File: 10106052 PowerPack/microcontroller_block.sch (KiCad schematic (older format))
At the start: 29 parts, among them J12 Molex_52207-1933_1x19-1MP_P1.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, J13 S5B-ZR-SM4A-TF, U4 PIC18F43K22T-IPT

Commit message: PowerPack schematic toplevel done
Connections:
- net DISCH_BAT1: no longer U4.23 (RA4/AN4/CAP3/QEB)
- new net DISCH_BAT2: U4.23 (RA4/AN4/CAP3/QEB)
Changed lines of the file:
@@
 $Descr A4 11693 8268
 encoding utf-8
-Sheet 6 7
-Title ""
-Date ""
-Rev ""
+Sheet 4 4
+Title "Microcontroller block"
+Date "2020-04-05"
+Rev "1"
 Comp ""
 Comment1 ""
@@
 $EndComp
 $Comp
-L 10106052_PowerPack:+VDC_PERM #PWR?
+L 10106052_PowerPack:+VDC_PERM #PWR0132
 U 1 1 5E9422DF
 P 10350 3450
-F 0 "#PWR?" H 10350 3300 50  0001 C CNN
+F 0 "#PWR0132" H 10350 3300 50  0001 C CNN
 F 1 "+VDC_PERM" V 10365 3577 50  0000 L CNN
 F 2 "" H 10350 3450 50  0001 C CNN
@@
 $EndComp
 $Comp
-L power:+5V #PWR?
+L power:+5V #PWR0133
 U 1 1 5E942FF6
 P 10350 3250
-F 0 "#PWR?" H 10350 3100 50  0001 C CNN
+F 0 "#PWR0133" H 10350 3100 50  0001 C CNN
 F 1 "+5V" V 10365 3378 50  0000 L CNN
 F 2 "" H 10350 3250 50  0001 C CNN
@@
 $EndComp
 $Comp
-L power:GND #PWR?
+L power:GND #PWR0134
 U 1 1 5E958B97
 P 10250 2350
-F 0 "#PWR?" H 10250 2100 50  0001 C CNN
+F 0 "#PWR0134" H 10250 2100 50  0001 C CNN
 F 1 "GND" V 10255 2222 50  0000 R CNN
 F 2 "" H 10250 2350 50  0001 C CNN
@@
 $EndComp
 $Comp
-L power:GND #PWR?
+L power:GND #PWR0135
 U 1 1 5E951987
 P 10550 6100
-F 0 "#PWR?" H 10550 5850 50  0001 C CNN
+F 0 "#PWR0135" H 10550 5850 50  0001 C CNN
 F 1 "GND" H 10555 5927 50  0000 C CNN
 F 2 "" H 10550 6100 50  0001 C CNN
@@
 $EndComp
 $Comp
-L power:GND #PWR?
+L power:GND #PWR0136
 U 1 1 5E944184
 P 7400 6150
-F 0 "#PWR?" H 7400 5900 50  0001 C CNN
+F 0 "#PWR0136" H 7400 5900 50  0001 C CNN
 F 1 "GND" H 7405 5977 50  0000 C CNN
 F 2 "" H 7400 6150 50  0001 C CNN
@@
 $EndComp
 $Comp
-L power:GNDA #PWR?
+L power:GNDA #PWR0137
 U 1 1 5E93FC0C
 P 9450 6100
-F 0 "#PWR?" H 9450 5850 50  0001 C CNN
+F 0 "#PWR0137" H 9450 5850 50  0001 C CNN
 F 1 "GNDA" H 9455 5927 50  0000 C CNN
 F 2 "" H 9450 6100 50  0001 C CNN
@@
 $EndComp
 $Comp
-L 10106052_PowerPack:+3.0VREF #PWR?
+L 10106052_PowerPack:+3.0VREF #PWR0138
 U 1 1 5EA046DC
 P 2300 4350
-F 0 "#PWR?" H 2300 4200 50  0001 C CNN
+F 0 "#PWR0138" H 2300 4200 50  0001 C CNN
 F 1 "+3.0VREF" V 2315 4478 50  0000 L CNN
 F 2 "" H 2300 4350 50  0001 C CNN
@@
 $EndComp
 $Comp
-L power:+5V #PWR?
+L power:+5V #PWR0139
 U 1 1 5EA2A611
 P 1400 1600
-F 0 "#PWR?" H 1400 1450 50  0001 C CNN
+F 0 "#PWR0139" H 1400 1450 50  0001 C CNN
 F 1 "+5V" H 1415 1773 50  0000 C CNN
 F 2 "" H 1400 1600 50  0001 C CNN
@@
 $EndComp
 $Comp
-L power:+5V #PWR?
+L power:+5V #PWR0140
 U 1 1 5EA4D723
 P 5200 1000
-F 0 "#PWR?" H 5200 850 50  0001 C CNN
+F 0 "#PWR0140" H 5200 850 50  0001 C CNN
 F 1 "+5V" H 5215 1173 50  0000 C CNN
 F 2 "" H 5200 1000 50  0001 C CNN
@@
 $EndComp
 $Comp
-L power:GND #PWR?
+L power:GND #PWR0141
 U 1 1 5EA9900D
 P 5200 2000
-F 0 "#PWR?" H 5200 1750 50  0001 C CNN
+F 0 "#PWR0141" H 5200 1750 50  0001 C CNN
 F 1 "GND" H 5205 1827 50  0000 C CNN
 F 2 "" H 5200 2000 50  0001 C CNN
@@
 $EndComp
 $Comp
-L power:GND #PWR?
+L power:GND #PWR0142
 U 1 1 5EAA1DDD
 P 3800 4950
-F 0 "#PWR?" H 3800 4700 50  0001 C CNN
+F 0 "#PWR0142" H 3800 4700 50  0001 C CNN
 F 1 "GND" H 3805 4777 50  0000 C CNN
 F 2 "" H 3800 4950 50  0001 C CNN
@@
 $EndComp
 $Comp
-L power:GND #PWR?
+L power:GND #PWR0143
 U 1 1 5EAE8BC9
 P 1150 4500
-F 0 "#PWR?" H 1150 4250 50  0001 C CNN
+F 0 "#PWR0143" H 1150 4250 50  0001 C CNN
 F 1 "GND" H 1155 4327 50  0000 C CNN
 F 2 "" H 1150 4500 50  0001 C CNN
@@
 $EndComp
 $Comp
-L power:+5V #PWR?
+L power:+5V #PWR0144
 U 1 1 5EAF26B7
 P 1250 3250
-F 0 "#PWR?" H 1250 3100 50  0001 C CNN
+F 0 "#PWR0144" H 1250 3100 50  0001 C CNN
 F 1 "+5V" H 1265 3423 50  0000 C CNN
 F 2 "" H 1250 3250 50  0001 C CNN
@@
 CHARG_BAT2
 Text HLabel 5400 4350 2    50   Output ~ 0
-DISCH_BAT1
+DISCH_BAT2
 Text HLabel 5800 2450 2    50   Output ~ 0
 ID_BAT_READ
@@
 Text HLabel 8850 3350 0    50   Output ~ 0
 BP
-Text HLabel 8950 5250 0    50   Output ~ 0
-BP_INFO
 Text HLabel 2250 2500 0    50   Input ~ 0
 TEMP_MEAS
@@
 Text HLabel 2250 2700 0    50   Output ~ 0
 V_EN
-Text HLabel 2250 3050 0    50   Input ~ 0
-BP_INFO
 Text HLabel 2250 3150 0    50   Input ~ 0
 TEMP_BAT2
@@
 Connection ~ 1650 3850
 Connection ~ 1400 3950
+Text Label 8950 5250 2    50   ~ 0
+BP_INFO
+Text Label 2250 3050 2    50   ~ 0
+BP_INFO
 $EndSCHEMATC

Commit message: Added ICSP Prog label
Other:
- note added: "ICSP Prog"
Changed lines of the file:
@@
 Text Label 2250 3050 2    50   ~ 0
 BP_INFO
+Text Notes 650  4150 1    50   ~ 10
+ICSP Prog
 $EndSCHEMATC

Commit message: Added parameters to components
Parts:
- C22: value 10uF -> 10u; Note (none) -> BOM lists C0603C106M9PACTM but only TU was found
- C23, C24, C25: value 100nF -> 100n
- D14: Manufacturer ST Micro -> STMicroelectronics
- J13: footprint (none) -> Connector_JST:JST_EH_S5B-EH_1x05_P2.50mm_Horizontal
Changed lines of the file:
@@
 F 1 "SMA6J28A" V 10595 5629 50  0000 L CNN
 F 2 "Diode_SMD:D_SMA" H 10550 5350 50  0001 C CNN
-F 3 "https://www.st.com/content/ccc/resource/technical/document/datasheet/56/26/d7/6f/22/8c/4e/b3/CD00152688.pdf/files/CD00152688.pdf/_jcr_content/translations/en.CD00152688.pdf" H 10500 5550 50  0001 C CNN
+F 3 "http://www.st.com/content/ccc/resource/technical/document/datasheet/56/26/d7/6f/22/8c/4e/b3/CD00152688.pdf/files/CD00152688.pdf/_jcr_content/translations/en.CD00152688.pdf" H 10500 5550 50  0001 C CNN
 F 4 "DIODE TRANSIL 33V, SMA" H 10504 5729 50  0001 C CNN "Description"
 F 5 "10060347" H 10504 5729 50  0001 C CNN "Item Number"
-F 6 "ST Micro" V 10641 5629 50  0001 L CNN "Manufacturer"
+F 6 "STMicroelectronics" V 10641 5629 50  0001 L CNN "Manufacturer"
 F 7 "SMA6J28A-TR" V 10686 5629 50  0001 L CNN "Manufacturer_No"
 	1    10550 5550
@@
 P 9200 5550
 F 0 "C25" H 9315 5596 50  0000 L CNN
-F 1 "100nF" H 9315 5505 50  0000 L CNN
+F 1 "100n" H 9315 5505 50  0000 L CNN
 F 2 "Capacitor_SMD:C_0603_1608Metric" H 9238 5400 50  0001 C CNN
 F 3 "https://api.kemet.com/component-edge/download/datasheet/C0603C104K5RACTU.pdf" H 9200 5550 50  0001 C CNN
@@
 P 5200 1600
 F 0 "C24" H 5315 1646 50  0000 L CNN
-F 1 "100nF" H 5315 1555 50  0000 L CNN
+F 1 "100n" H 5315 1555 50  0000 L CNN
 F 2 "Capacitor_SMD:C_0603_1608Metric" H 5238 1450 50  0001 C CNN
 F 3 "https://api.kemet.com/component-edge/download/datasheet/C0603C104K5RACTU.pdf" H 5200 1600 50  0001 C CNN
@@
 P 4750 1600
 F 0 "C23" H 4865 1646 50  0000 L CNN
-F 1 "100nF" H 4865 1555 50  0000 L CNN
+F 1 "100n" H 4865 1555 50  0000 L CNN
 F 2 "Capacitor_SMD:C_0603_1608Metric" H 4788 1450 50  0001 C CNN
 F 3 "https://api.kemet.com/component-edge/download/datasheet/C0603C104K5RACTU.pdf" H 4750 1600 50  0001 C CNN
@@
 P 4300 1600
 F 0 "C22" H 4415 1646 50  0000 L CNN
-F 1 "10uF" H 4415 1555 50  0000 L CNN
+F 1 "10u" H 4415 1555 50  0000 L CNN
 F 2 "Capacitor_SMD:C_0603_1608Metric" H 4338 1450 50  0001 C CNN
-F 3 "https://api.kemet.com/component-edge/download/datasheet/C0603C104K5RACTU.pdf" H 4300 1600 50  0001 C CNN
+F 3 "https://api.kemet.com/component-edge/download/datasheet/C0603C106M9PACTU.pdf" H 4300 1600 50  0001 C CNN
 F 4 "CAPACITOR CERAMIC 10UF 6.3V 20% X5R 0603" H 4415 1746 50  0001 C CNN "Description"
 F 5 "10021370" H 4415 1746 50  0001 C CNN "Item Number"
 F 6 "Kemet" H 4300 1600 50  0001 C CNN "Manufacturer"
 F 7 "C0603C106M9PACTM" H 4300 1600 50  0001 C CNN "Manufacturer_No"
+F 8 "BOM lists C0603C106M9PACTM but only TU was found" H 4300 1600 50  0001 C CNN "Note"
 	1    4300 1600
 	1    0    0    -1
@@
 F 0 "J13" H 668 3525 50  0000 C CNN
 F 1 "S5B-ZR-SM4A-TF" H 668 3616 50  0000 C CNN
-F 2 "" H 750 3950 50  0001 C CNN
+F 2 "Connector_JST:JST_EH_S5B-EH_1x05_P2.50mm_Horizontal" H 750 3950 50  0001 C CNN
 F 3 "http://www.jst-mfg.com/product/pdf/eng/eZH.pdf" H 750 3950 50  0001 C CNN
 F 4 "1x5, 1.5mm pitch, RA TH Shrouded Header" H 750 3950 50  0001 C CNN "Description"

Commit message: Footprints relinked
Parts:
- C22, C23, C24, C25: footprint Capacitor_SMD:C_0603_1608Metric -> 10106052 PowerPack:CAPC1608X86N
- D10, D11, D12, D13: footprint Package_SO:SC-74-6_1.5x2.9mm_P0.95mm -> 10106052 PowerPack:SOT95P275X110-6N
- D14: footprint Diode_SMD:D_SMA -> 10106052 PowerPack:DIOM5126X203N_SWP
- J12: footprint (none) -> 10106052 PowerPack:CON-52207-1960
- J13: footprint Connector_JST:JST_EH_S5B-EH_1x05_P2.50mm_Horizontal -> 10106052 PowerPack:CON-S5B-ZR-SM4A-TF
- R33, R34, R35, R36, R37, R38, R39, R40, R41, R42, R43, R45, R46, R47, R48, R49: footprint Resistor_SMD:R_0603_1608Metric -> 10106052 PowerPack:RESC1608X50AN
- R44: footprint Resistor_SMD:R_1206_3216Metric -> 10106052 PowerPack:RESC3216X60N
- U4: footprint Package_QFP:TQFP-44_10x10mm_P0.8mm -> 10106052 PowerPack:QFP80P1200X1200X120-44N

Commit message: Added 3D Models, corrected orientation of parts on schematic, added TX/RX TP
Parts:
- added RX, TX: TestPoint, 10106052 PowerPack:TP-40R-NSA, symbol Connector:TestPoint
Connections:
- net +5V: now also C22.2, C23.2, C24.2; no longer C22.1, C23.1, C24.1
- net +VDC_PERM: now also D14.2 (K)
- net BP: now also R48.2
- net BP_INFO: now also C25.2; no longer C25.1
- net GND: now also C22.1, C23.1, C24.1; no longer C22.2, C23.2, C24.2
- net GNDA: now also C25.1; no longer C25.2
- net RX: now also RX.1
- net TX: now also TX.1
- net at D11.3 (K2), J12.5 (Pin_5), R42.1: no longer R48.2
- net at D11.4 (K3), J12.4 (Pin_4), R43.1: no longer D14.2 (K)
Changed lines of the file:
@@
 F 7 "C0603C104K5RACTU" H 9200 5550 50  0001 C CNN "Manufacturer_No"
 	1    9200 5550
-	1    0    0    -1
+	-1   0    0    1
 $EndComp
 $Comp
@@
 F 7 "C0603C104K5RACTU" H 5200 1600 50  0001 C CNN "Manufacturer_No"
 	1    5200 1600
-	1    0    0    -1
+	-1   0    0    1
 $EndComp
 $Comp
@@
 F 7 "C0603C104K5RACTU" H 4750 1600 50  0001 C CNN "Manufacturer_No"
 	1    4750 1600
-	1    0    0    -1
+	-1   0    0    1
 $EndComp
 $Comp
@@
 F 8 "BOM lists C0603C106M9PACTM but only TU was found" H 4300 1600 50  0001 C CNN "Note"
 	1    4300 1600
-	1    0    0    -1
+	-1   0    0    1
 $EndComp
 $Comp
@@
 Text HLabel 2250 2600 0    50   Input ~ 0
 V_CH
-Text HLabel 2250 2900 0    50   Input ~ 0
+Text HLabel 1650 2900 0    50   Input ~ 0
 RX
-Text HLabel 2250 2800 0    50   Output ~ 0
+Text HLabel 1650 2800 0    50   Output ~ 0
 TX
 Text HLabel 2250 2700 0    50   Output ~ 0
@@
 	6800 3750 6800 3350
 Wire Wire Line
-	10600 3850 10550 3850
-Wire Wire Line
 	6700 3450 6700 3850
 Wire Wire Line
@@
 	10400 2350 10250 2350
 Wire Wire Line
-	10600 3750 9700 3750
-Wire Wire Line
 	10600 3950 6800 3950
 Wire Wire Line
@@
 	10600 4150 6400 4150
 Wire Wire Line
-	10550 5400 10550 3850
-Wire Wire Line
 	10550 6100 10550 5700
 Wire Wire Line
@@
 	9700 5400 9700 5250
 Wire Wire Line
-	9700 4800 9700 3750
-Wire Wire Line
-	9700 3750 7000 3750
-Wire Wire Line
-	10550 3850 6900 3850
-Wire Wire Line
-	10350 3450 10600 3450
-Wire Wire Line
-	8850 3350 10600 3350
+	10350 3450 10550 3450
+Wire Wire Line
+	8850 3350 9700 3350
 Wire Wire Line
 	8200 2550 8200 5500
@@
 Wire Wire Line
 	2600 2700 2250 2700
-Wire Wire Line
-	2600 2800 2250 2800
-Wire Wire Line
-	2600 2900 2250 2900
 Wire Wire Line
 	2600 3050 2250 3050
@@
 Connection ~ 9200 5250
 Connection ~ 9700 5250
-Connection ~ 9700 3750
-Connection ~ 10550 3850
 Connection ~ 7400 3150
 Connection ~ 7500 3050
@@
 Text Notes 650  4150 1    50   ~ 10
 ICSP Prog
+Wire Wire Line
+	7000 3750 10600 3750
+Wire Wire Line
+	9700 3350 9700 4800
+Connection ~ 9700 3350
+Wire Wire Line
+	9700 3350 10600 3350
+Wire Wire Line
+	6900 3850 10600 3850
+Wire Wire Line
+	10550 5400 10550 3450
+Connection ~ 10550 3450
+Wire Wire Line
+	10550 3450 10600 3450
+$Comp
+L Connector:TestPoint TX
+U 1 1 5ED5F142
+P 1850 2150
+F 0 "TX" H 1800 2350 50  0000 L CNN
+F 1 "TestPoint" H 1908 2177 50  0001 L CNN
+F 2 "10106052 PowerPack:TP-40R-NSA" H 2050 2150 50  0001 C CNN
+F 3 "~" H 2050 2150 50  0001 C CNN
+	1    1850 2150
+	1    0    0    -1
+$EndComp
+$Comp
+L Connector:TestPoint RX
+U 1 1 5ED5FB52
+P 2000 2150
+F 0 "RX" H 1950 2350 50  0000 L CNN
+F 1 "TestPoint" H 2058 2177 50  0001 L CNN
+F 2 "10106052 PowerPack:TP-40R-NSA" H 2200 2150 50  0001 C CNN
+F 3 "~" H 2200 2150 50  0001 C CNN
+	1    2000 2150
+	1    0    0    -1
+$EndComp
+Wire Wire Line
+	1650 2800 1850 2800
+Wire Wire Line
+	1650 2900 2000 2900
+Wire Wire Line
+	1850 2150 1850 2800
+Connection ~ 1850 2800
+Wire Wire Line
+	1850 2800 2600 2800
+Wire Wire Line
+	2000 2150 2000 2900
+Connection ~ 2000 2900
+Wire Wire Line
+	2000 2900 2600 2900
 $EndSCHEMATC

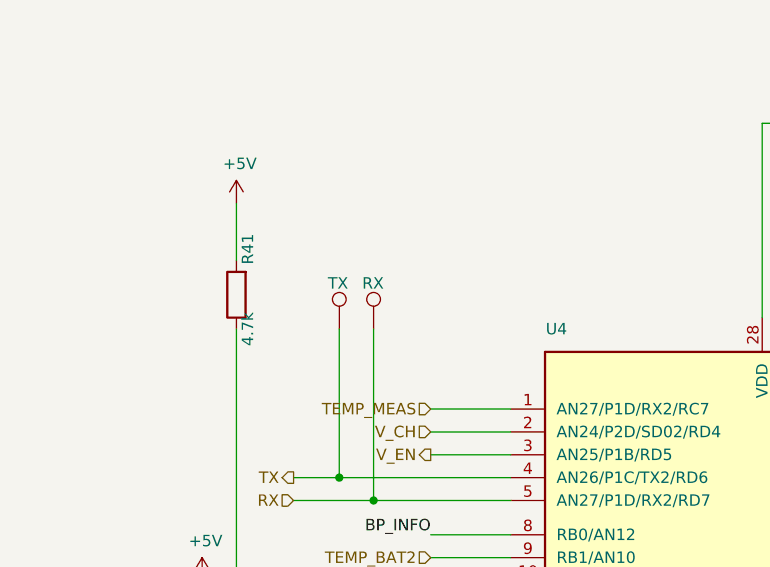
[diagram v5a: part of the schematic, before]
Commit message: Corrected BNX00201 and SUD50P06-15L-E3 Symbols to Match Footprint
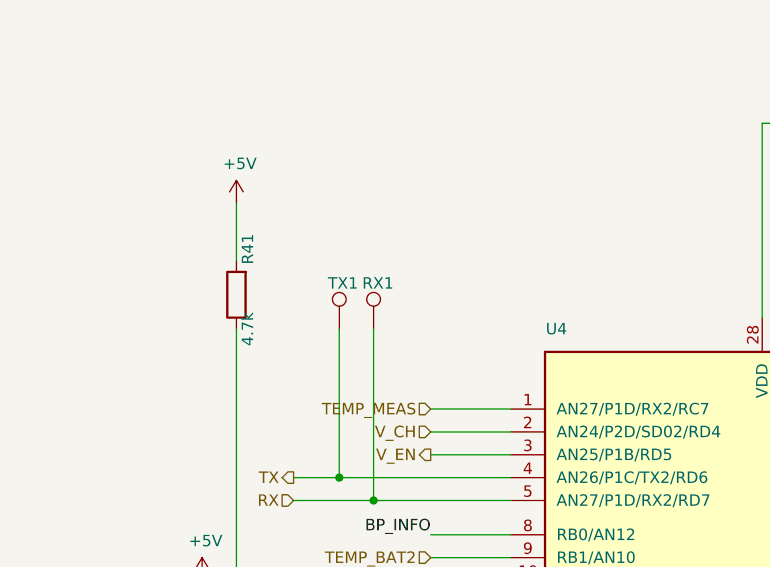
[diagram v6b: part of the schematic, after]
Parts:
- renumbered RX to RX1, TX to TX1
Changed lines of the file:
@@
 	10550 3450 10600 3450
 $Comp
-L Connector:TestPoint TX
+L Connector:TestPoint TX1
 U 1 1 5ED5F142
 P 1850 2150
-F 0 "TX" H 1800 2350 50  0000 L CNN
+F 0 "TX1" H 1800 2350 50  0000 L CNN
 F 1 "TestPoint" H 1908 2177 50  0001 L CNN
 F 2 "10106052 PowerPack:TP-40R-NSA" H 2050 2150 50  0001 C CNN
@@
 $EndComp
 $Comp
-L Connector:TestPoint RX
+L Connector:TestPoint RX1
 U 1 1 5ED5FB52
 P 2000 2150
-F 0 "RX" H 1950 2350 50  0000 L CNN
+F 0 "RX1" H 1950 2350 50  0000 L CNN
 F 1 "TestPoint" H 2058 2177 50  0001 L CNN
 F 2 "10106052 PowerPack:TP-40R-NSA" H 2200 2150 50  0001 C CNN

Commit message: powerpack-dev
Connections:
- net RX: no longer names the net of RX1.1, U4.5 (AN27/P1D/RX2/RD7)
- net TX: no longer names the net of TX1.1, U4.4 (AN26/P1C/TX2/RD6)
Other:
- moved on the sheet: RX1, TX1
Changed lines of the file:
@@
 U 1 1 5E8821B6
 P 1400 2000
-F 0 "R41" V 1350 1800 50  0000 C CNN
-F 1 "4.7k" V 1350 2150 50  0000 C CNN
+F 0 "R41" H 1470 1954 50  0000 L CNN
+F 1 "4.7k" H 1470 2045 50  0000 L CNN
 F 2 "10106052 PowerPack:RESC1608X50AN" V 1330 2000 50  0001 C CNN
 F 3 "https://www.yageo.com/upload/media/product/productsearch/datasheet/rchip/PYu-RC_Group_51_RoHS_L_10.pdf" H 1400 2000 50  0001 C CNN
@@
 U 1 1 5E934E22
 P 9700 5550
-F 0 "R49" V 9650 5350 50  0000 C CNN
-F 1 "10k" V 9650 5700 50  0000 C CNN
+F 0 "R49" H 9630 5504 50  0000 R CNN
+F 1 "10k" H 9630 5595 50  0000 R CNN
 F 2 "10106052 PowerPack:RESC1608X50AN" V 9630 5550 50  0001 C CNN
 F 3 "https://www.yageo.com/upload/media/product/productsearch/datasheet/rchip/PYu-RC_Group_51_RoHS_L_10.pdf" H 9700 5550 50  0001 C CNN
@@
 U 1 1 5E933AAF
 P 9700 4950
-F 0 "R48" V 9650 4750 50  0000 C CNN
-F 1 "62k" V 9650 5100 50  0000 C CNN
+F 0 "R48" H 9630 4904 50  0000 R CNN
+F 1 "62k" H 9630 4995 50  0000 R CNN
 F 2 "10106052 PowerPack:RESC1608X50AN" V 9630 4950 50  0001 C CNN
 F 3 "https://www.yageo.com/upload/media/product/productsearch/datasheet/rchip/PYu-RC_Group_51_RoHS_L_10.pdf" H 9700 4950 50  0001 C CNN
@@
 Text HLabel 2250 2600 0    50   Input ~ 0
 V_CH
-Text HLabel 1650 2900 0    50   Input ~ 0
-RX
-Text HLabel 1650 2800 0    50   Output ~ 0
-TX
 Text HLabel 2250 2700 0    50   Output ~ 0
 V_EN
@@
 L Connector:TestPoint TX1
 U 1 1 5ED5F142
-P 1850 2150
-F 0 "TX1" H 1800 2350 50  0000 L CNN
-F 1 "TestPoint" H 1908 2177 50  0001 L CNN
-F 2 "10106052 PowerPack:TP-40R-NSA" H 2050 2150 50  0001 C CNN
-F 3 "~" H 2050 2150 50  0001 C CNN
-	1    1850 2150
+P 1625 2150
+F 0 "TX1" H 1575 2350 50  0000 L CNN
+F 1 "TestPoint" H 1683 2177 50  0001 L CNN
+F 2 "10106052 PowerPack:TP-40R-NSA" H 1825 2150 50  0001 C CNN
+F 3 "~" H 1825 2150 50  0001 C CNN
+	1    1625 2150
 	1    0    0    -1
 $EndComp
@@
 L Connector:TestPoint RX1
 U 1 1 5ED5FB52
-P 2000 2150
-F 0 "RX1" H 1950 2350 50  0000 L CNN
-F 1 "TestPoint" H 2058 2177 50  0001 L CNN
-F 2 "10106052 PowerPack:TP-40R-NSA" H 2200 2150 50  0001 C CNN
-F 3 "~" H 2200 2150 50  0001 C CNN
-	1    2000 2150
+P 1775 2150
+F 0 "RX1" H 1725 2350 50  0000 L CNN
+F 1 "TestPoint" H 1833 2177 50  0001 L CNN
+F 2 "10106052 PowerPack:TP-40R-NSA" H 1975 2150 50  0001 C CNN
+F 3 "~" H 1975 2150 50  0001 C CNN
+	1    1775 2150
 	1    0    0    -1
 $EndComp
 Wire Wire Line
-	1650 2800 1850 2800
-Wire Wire Line
-	1650 2900 2000 2900
-Wire Wire Line
-	1850 2150 1850 2800
-Connection ~ 1850 2800
-Wire Wire Line
-	1850 2800 2600 2800
-Wire Wire Line
-	2000 2150 2000 2900
-Connection ~ 2000 2900
-Wire Wire Line
-	2000 2900 2600 2900
+	1625 2150 1625 2800
+Wire Wire Line
+	1775 2150 1775 2900
+Wire Wire Line
+	1625 2800 2600 2800
+Wire Wire Line
+	1775 2900 2600 2900
 $EndSCHEMATC

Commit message: move all fps to global libraries
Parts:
- C22, C23, C24, C25: footprint 10106052 PowerPack:CAPC1608X86N -> AllModules:CAPC1608X86N
- D10, D11, D12, D13: footprint 10106052 PowerPack:SOT95P275X110-6N -> AllModules:SOT95P275X110-6N
- D14: footprint 10106052 PowerPack:DIOM5126X203N_SWP -> AllModules:DIOM5126X203N_SWP
- J12: footprint 10106052 PowerPack:CON-52207-1960 -> AllModules:CON-52207-1960
- J13: footprint 10106052 PowerPack:CON-S5B-ZR-SM4A-TF -> AllModules:CON-S5B-ZR-SM4A-TF
- R33, R34, R35, R36, R37, R38, R39, R40, R41, R42, R43, R45, R46, R47, R48, R49: footprint 10106052 PowerPack:RESC1608X50AN -> AllModules:RESC1608X50AN
- R44: footprint 10106052 PowerPack:RESC3216X60N -> AllModules:RESC3216X60N
- RX1, TX1: footprint 10106052 PowerPack:TP-40R-NSA -> AllModules:TP-40R-NSA
- U4: footprint 10106052 PowerPack:QFP80P1200X1200X120-44N -> AllModules:QFP80P1200X1200X120-44N
